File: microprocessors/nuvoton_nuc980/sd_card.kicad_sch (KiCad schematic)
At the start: 1 part, among them J3 MSD-4-A

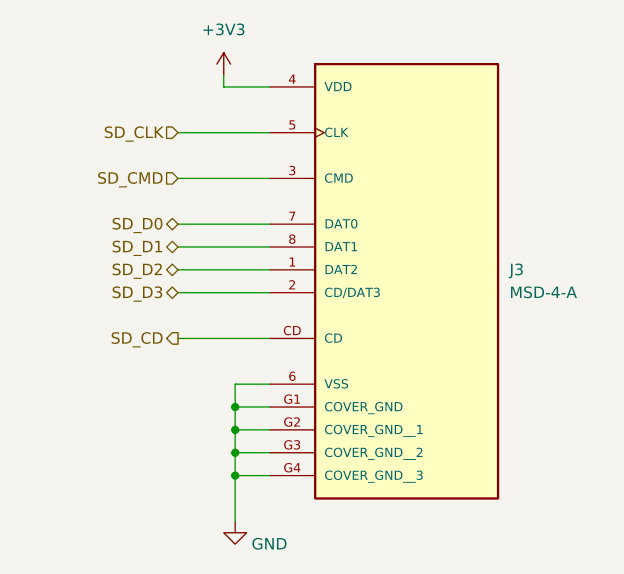
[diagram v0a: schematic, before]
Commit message: feat: ERC passing cotti-nuvoton
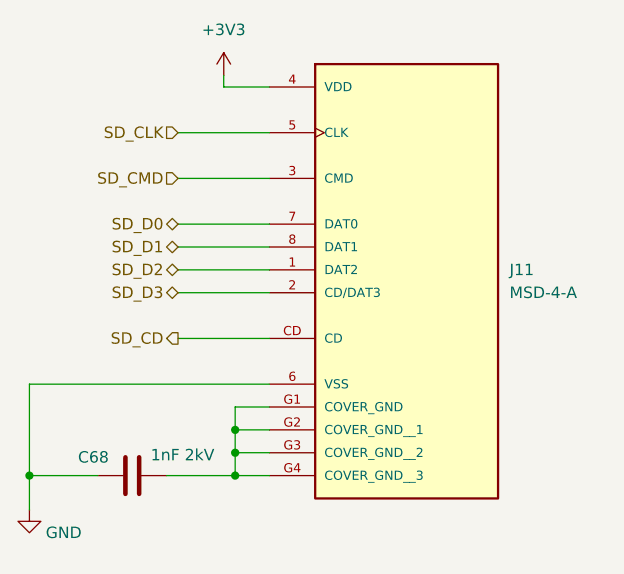
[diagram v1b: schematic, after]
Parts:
- removed J3: MSD-4-A, project_footprints:CUI_MSD-4-A, symbol project_symbols:MSD-4-A
- added C68: 1nF 2kV, Capacitor_SMD:C_1206_3216Metric_Pad1.33x1.80mm_HandSolder, symbol Device:C
- added J11: MSD-4-A, cotti_footprints:CUI_MSD-4-A, symbol cotti_connectors:MSD-4-A
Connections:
- net +3V3: now also J11.4 (VDD)
- net GND: now also C68.1, J11.6 (VSS)
- net SD_CD: now also J11.CD
- net SD_CLK: now also J11.5 (CLK)
- net SD_CMD: now also J11.3 (CMD)
- net SD_D0: now also J11.7 (DAT0)
- net SD_D1: now also J11.8 (DAT1)
- net SD_D2: now also J11.1 (DAT2)
- net SD_D3: now also J11.2 (CD/DAT3)
- new net: C68.2, J11.G1 (COVER_GND), J11.G2 (COVER_GND__1), J11.G3 (COVER_GND__2), J11.G4 (COVER_GND__3)
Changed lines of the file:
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@@
 	)
 	(junction
-		(at 110.49 95.25)
+		(at 87.63 102.87)
+		(diameter 0)
+		(color 0 0 0 0)
+	)
+	(junction
+		(at 110.49 102.87)
 		(diameter 0)
 		(color 0 0 0 0)
@@
 		(color 0 0 0 0)
 	)
-	(junction
-		(at 110.49 102.87)
-		(diameter 0)
-		(color 0 0 0 0)
-	)
-	(wire
-		(pts
-			(xy 110.49 92.71) (xy 110.49 95.25)
-		)
-		(stroke
-			(width 0)
-			(type default)
-		)
-	)
 	(wire
 		(pts
@@
 	(wire
 		(pts
+			(xy 87.63 102.87) (xy 95.25 102.87)
+		)
+		(stroke
+			(width 0)
+			(type default)
+		)
+	)
+	(wire
+		(pts
 			(xy 110.49 100.33) (xy 114.3 100.33)
 		)
@@
 	(wire
 		(pts
+			(xy 102.87 102.87) (xy 110.49 102.87)
+		)
+		(stroke
+			(width 0)
+			(type default)
+		)
+	)
+	(wire
+		(pts
+			(xy 87.63 102.87) (xy 87.63 106.68)
+		)
+		(stroke
+			(width 0)
+			(type default)
+		)
+	)
+	(wire
+		(pts
 			(xy 104.14 82.55) (xy 114.3 82.55)
 		)
@@
 	(wire
 		(pts
-			(xy 110.49 102.87) (xy 110.49 107.95)
+			(xy 87.63 92.71) (xy 87.63 102.87)
 		)
 		(stroke
@@
 	(wire
 		(pts
-			(xy 114.3 92.71) (xy 110.49 92.71)
+			(xy 87.63 92.71) (xy 114.3 92.71)
 		)
 		(stroke
@@
 	)
 	(symbol
+		(lib_id "Device:C")
+		(at 99.06 102.87 90)
+		(unit 1)
+		(exclude_from_sim no)
+		(in_bom yes)
+		(on_board yes)
+		(dnp no)
+		(property "Reference" "C68"
+			(at 94.742 100.838 90)
+			(effects
+				(font
+					(size 1.27 1.27)
+				)
+			)
+		)
+		(property "Value" "1nF 2kV"
+			(at 104.648 100.584 90)
+			(effects
+				(font
+					(size 1.27 1.27)
+				)
+			)
+		)
+		(property "Footprint" "Capacitor_SMD:C_1206_3216Metric_Pad1.33x1.80mm_HandSolder"
+			(at 102.87 101.9048 0)
+			(effects
+				(font
+					(size 1.27 1.27)
+				)
+				(hide yes)
+			)
+		)
+		(property "Datasheet" "http://www.passivecomponent.com/wp-content/uploads/datasheet/WTC_MLCC_Middle_and_High_Voltage.pdf"
+			(at 99.06 102.87 0)
+			(effects
+				(font
+					(size 1.27 1.27)
+				)
+				(hide yes)
+			)
+		)
+		(property "Description" "Unpolarized capacitor"
+			(at 99.06 102.87 0)
+			(effects
+				(font
+					(size 1.27 1.27)
+				)
+				(hide yes)
+			)
+		)
+		(property "Digikey" "https://www.digikey.com/en/products/detail/walsin-technology-corporation/1206B102M202CT/15791323"
+			(at 99.06 102.87 90)
+			(effects
+				(font
+					(size 1.27 1.27)
+				)
+				(hide yes)
+			)
+		)
+		(property "Mfr." "Walsin Technology Corporation"
+			(at 99.06 102.87 90)
+			(effects
+				(font
+					(size 1.27 1.27)
+				)
+				(hide yes)
+			)
+		)
+		(property "Mfr. P/N" "1206B102M202CT"
+			(at 99.06 102.87 90)
+			(effects
+				(font
+					(size 1.27 1.27)
+				)
+				(hide yes)
+			)
+		)
+		(property "Sim.Pins" ""
+			(at 99.06 102.87 90)
+			(effects
+				(font
+					(size 1.27 1.27)
+				)
+				(hide yes)
+			)
+		)
+		(pin "2"
+		)
+		(pin "1"
+		)
+		(instances
+			(project "nuvoton_nuc980"
+				(path "/109442c7-6d61-4448-a955-a6cd87e17c77/1953f6ba-660a-47c3-9a25-fc45adb7c5a8"
+					(reference "C68")
+					(unit 1)
+				)
+			)
+		)
+	)
+	(symbol
 		(lib_id "power:GND")
-		(at 110.49 107.95 0)
+		(at 87.63 106.68 0)
 		(unit 1)
 		(exclude_from_sim no)
@@
 		(dnp no)
 		(property "Reference" "#PWR074"
-			(at 110.49 114.3 0)
+			(at 87.63 113.03 0)
 			(effects
 				(font
@@
 		)
 		(property "Value" "GND"
-			(at 114.3 110.49 0)
+			(at 91.44 109.22 0)
 			(effects
 				(font
@@
 		)
 		(property "Footprint" ""
-			(at 110.49 107.95 0)
+			(at 87.63 106.68 0)
 			(effects
 				(font
@@
 		)
 		(property "Datasheet" ""
-			(at 110.49 107.95 0)
+			(at 87.63 106.68 0)
 			(effects
 				(font
@@
 		)
 		(property "Description" "Power symbol creates a global label with name \"GND\" , ground"
-			(at 110.49 107.95 0)
+			(at 87.63 106.68 0)
 			(effects
 				(font
@@
 	)
 	(symbol
-		(lib_id "project_symbols:MSD-4-A")
+		(lib_id "cotti_connectors:MSD-4-A")
 		(at 129.54 77.47 0)
 		(unit 1)
@@
 		(dnp no)
 		(fields_autoplaced yes)
-		(property "Reference" "J3"
+		(property "Reference" "J11"
 			(at 140.97 80.0099 0)
 			(effects
@@
 			)
 		)
-		(property "Footprint" "project_footprints:CUI_MSD-4-A"
+		(property "Footprint" "cotti_footprints:CUI_MSD-4-A"
 			(at 128.524 37.084 0)
 			(effects
@@
 			)
 		)
+		(pin "1"
+		)
+		(pin "2"
+		)
+		(pin "6"
+		)
 		(pin "G2"
 		)
+		(pin "7"
+		)
+		(pin "G3"
+		)
+		(pin "3"
+		)
 		(pin "CD"
 		)
-		(pin "1"
-		)
-		(pin "2"
+		(pin "5"
+		)
+		(pin "4"
+		)
+		(pin "G1"
+		)
+		(pin "G4"
 		)
 		(pin "8"
 		)
-		(pin "5"
-		)
-		(pin "G1"
-		)
-		(pin "7"
-		)
-		(pin "6"
-		)
-		(pin "4"
-		)
-		(pin "G3"
-		)
-		(pin "3"
-		)
-		(pin "G4"
-		)
 		(instances
-			(project "nuvoton_nuc980"
+			(project ""
 				(path "/109442c7-6d61-4448-a955-a6cd87e17c77/1953f6ba-660a-47c3-9a25-fc45adb7c5a8"
-					(reference "J3")
+					(reference "J11")
 					(unit 1)
 				)
